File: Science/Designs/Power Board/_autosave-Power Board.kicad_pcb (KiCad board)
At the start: 2 copper layers, 114.3 x 90.2 mm, 27 parts, among them P1 PWR_IN, P2 MOTOR_PWR_OUT, P3 MAIN_PWR_OUT, P4 I2C, P5 MOTOR_SW, P6 REG_12V, P7 REG_5V, U1 INA219, U2 INA219, U3 INA219

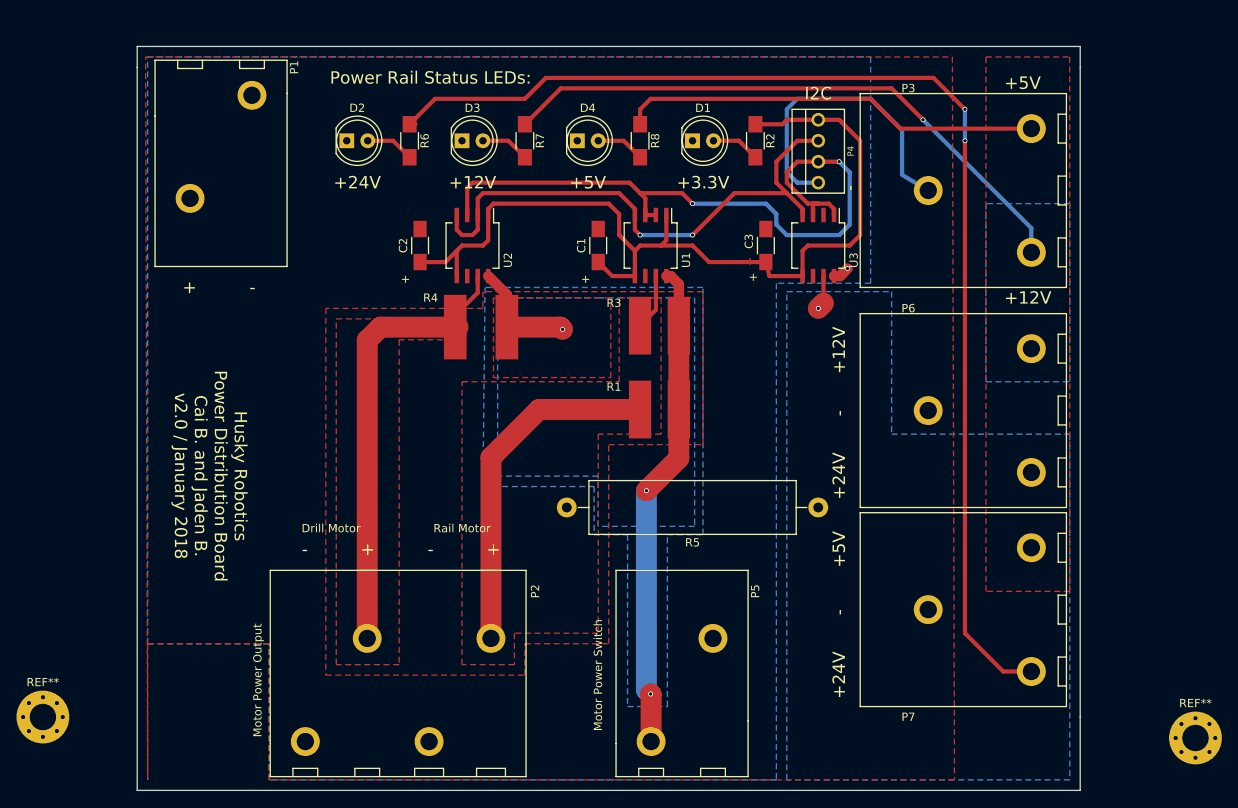
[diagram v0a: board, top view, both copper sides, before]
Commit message: Added mounting holes
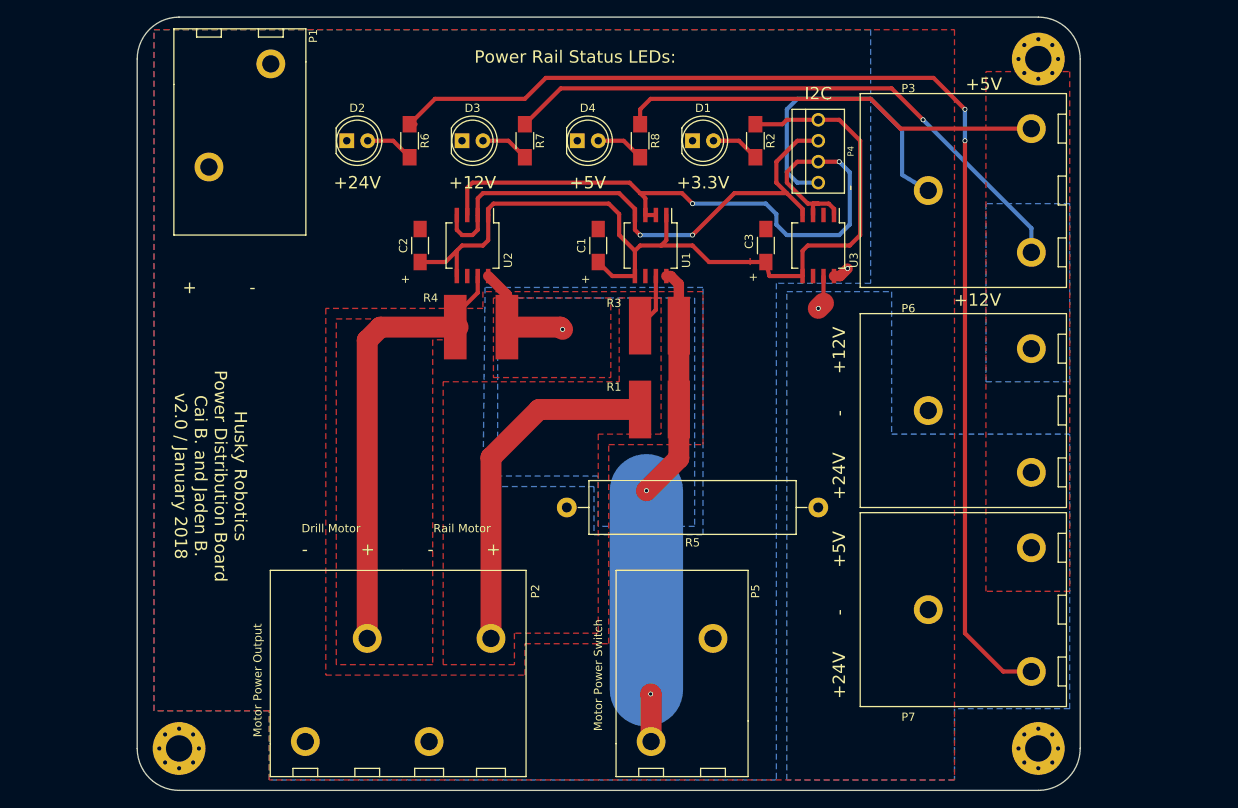
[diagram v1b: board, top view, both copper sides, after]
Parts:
- added REF**: MountingHole_3.2mm_M3_Pad_Via, Mounting_Holes:MountingHole_3.2mm_M3_Pad_Via, F.Cu at (182.9, 29.5)
- moved REF** 19.1 mm to (182.9, 113.0)
- moved REF** 16.9 mm to (78.7, 113.0)
- moved P1 4.44 mm to (86.1, 50.8)
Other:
- board size 114.3 x 90.2 mm -> 114.3 x 93.7 mm
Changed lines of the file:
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@@
     (links 60)
     (no_connects 0)
-    (area 73.584999 27.864999 188.035001 118.185001)
+    (area 73.584999 24.308999 188.035001 118.185001)
     (thickness 1.6)
-    (drawings 41)
+    (drawings 38)
     (tracks 172)
     (zones 0)
-    (modules 27)
+    (modules 28)
     (nets 16)
   )
@@
   (layers
     (0 F.Cu signal)
-    (31 B.Cu signal hide)
+    (31 B.Cu signal)
     (32 B.Adhes user hide)
     (33 F.Adhes user hide)
@@
   )
   (setup
-    (last_trace_width 2.54)
+    (last_trace_width 8.89)
     (user_trace_width 1.27)
     (user_trace_width 2.54)
@@
   )
   (module ScienceFootprints:PHOENIX_1792229 (layer F.Cu)
-    (at 83.82 54.61 180)
+    (at 86.106 50.8 180)
     (fp_text reference P1 (at -8.89 24.13 270) (layer F.SilkS)
       (effects (font (size 1 1) (thickness 0.15)))
@@
   )
   (module Mounting_Holes:MountingHole_3.2mm_M3_Pad_Via (layer F.Cu)
-    (at 62.23 109.22)
+    (at 78.74 113.03)
     (descr "Mounting Hole 3.2mm, M3")
     (tags "mounting hole 3.2mm m3")
     (attr virtual)
-    (fp_text reference REF** (at 0 -4.2) (layer F.SilkS)
+    (fp_text reference REF** (at 0 -4.2) (layer F.SilkS) hide
       (effects (font (size 1 1) (thickness 0.15)))
     )
@@
   )
   (module Mounting_Holes:MountingHole_3.2mm_M3_Pad_Via (layer F.Cu)
-    (at 201.93 111.76)
+    (at 182.88 113.03)
     (descr "Mounting Hole 3.2mm, M3")
     (tags "mounting hole 3.2mm m3")
     (attr virtual)
-    (fp_text reference REF** (at 0 -4.2) (layer F.SilkS)
+    (fp_text reference REF** (at 5.08 -2.794) (layer F.SilkS) hide
       (effects (font (size 1 1) (thickness 0.15)))
     )
@@
     (pad "" thru_hole circle (at 1.697056 -1.697056) (size 0.8 0.8) (drill 0.5) (layers *.Cu *.Mask))
   )
+  (module Mounting_Holes:MountingHole_3.2mm_M3_Pad_Via (layer F.Cu)
+    (at 182.88 29.464)
+    (descr "Mounting Hole 3.2mm, M3")
+    (tags "mounting hole 3.2mm m3")
+    (attr virtual)
+    (fp_text reference REF** (at 0 -4.2) (layer F.SilkS) hide
+      (effects (font (size 1 1) (thickness 0.15)))
+    )
+    (fp_text value MountingHole_3.2mm_M3_Pad_Via (at 0 4.2) (layer F.Fab)
+      (effects (font (size 1 1) (thickness 0.15)))
+    )
+    (fp_text user %R (at 0.3 0) (layer F.Fab)
+      (effects (font (size 1 1) (thickness 0.15)))
+    )
+    (fp_circle (center 0 0) (end 3.2 0) (layer Cmts.User) (width 0.15))
+    (fp_circle (center 0 0) (end 3.45 0) (layer F.CrtYd) (width 0.05))
+    (pad 1 thru_hole circle (at 0 0) (size 6.4 6.4) (drill 3.2) (layers *.Cu *.Mask))
+    (pad "" thru_hole circle (at 2.4 0) (size 0.8 0.8) (drill 0.5) (layers *.Cu *.Mask))
+    (pad "" thru_hole circle (at 1.697056 1.697056) (size 0.8 0.8) (drill 0.5) (layers *.Cu *.Mask))
+    (pad "" thru_hole circle (at 0 2.4) (size 0.8 0.8) (drill 0.5) (layers *.Cu *.Mask))
+    (pad "" thru_hole circle (at -1.697056 1.697056) (size 0.8 0.8) (drill 0.5) (layers *.Cu *.Mask))
+    (pad "" thru_hole circle (at -2.4 0) (size 0.8 0.8) (drill 0.5) (layers *.Cu *.Mask))
+    (pad "" thru_hole circle (at -1.697056 -1.697056) (size 0.8 0.8) (drill 0.5) (layers *.Cu *.Mask))
+    (pad "" thru_hole circle (at 0 -2.4) (size 0.8 0.8) (drill 0.5) (layers *.Cu *.Mask))
+    (pad "" thru_hole circle (at 1.697056 -1.697056) (size 0.8 0.8) (drill 0.5) (layers *.Cu *.Mask))
+  )
+  (gr_line (start 182.88 118.11) (end 78.74 118.11) (angle 90) (layer Edge.Cuts) (width 0.15))
+  (gr_line (start 187.96 29.464) (end 187.96 113.03) (angle 90) (layer Edge.Cuts) (width 0.15))
+  (gr_line (start 78.74 24.384) (end 182.88 24.384) (angle 90) (layer Edge.Cuts) (width 0.15))
+  (gr_line (start 73.66 113.03) (end 73.66 29.464) (angle 90) (layer Edge.Cuts) (width 0.15))
+  (gr_arc (start 78.74 29.464) (end 73.66 29.464) (angle 90) (layer Edge.Cuts) (width 0.15))
+  (gr_arc (start 182.88 29.464) (end 182.88 24.384) (angle 90) (layer Edge.Cuts) (width 0.15))
+  (gr_arc (start 182.88 113.03) (end 187.96 113.03) (angle 90) (layer Edge.Cuts) (width 0.15))
+  (gr_arc (start 78.74 113.03) (end 78.74 118.11) (angle 90) (layer Edge.Cuts) (width 0.15))
   (gr_text "Rail Motor" (at 113.03 86.36) (layer F.SilkS)
     (effects (font (size 1 1) (thickness 0.2)))
@@
     (effects (font (size 1.5 1.5) (thickness 0.3)))
   )
-  (gr_text "Power Rail Status LEDs:" (at 109.22 31.75) (layer F.SilkS)
+  (gr_text "Power Rail Status LEDs:" (at 126.746 29.21) (layer F.SilkS)
     (effects (font (size 1.5 1.5) (thickness 0.3)))
   )
@@
     (effects (font (size 1.5 1.5) (thickness 0.3)))
   )
-  (gr_text +12V (at 181.61 58.42) (layer F.SilkS)
-    (effects (font (size 1.5 1.5) (thickness 0.3)))
-  )
-  (gr_text +5V (at 180.975 32.385) (layer F.SilkS)
+  (gr_text +12V (at 175.514 58.674) (layer F.SilkS)
+    (effects (font (size 1.5 1.5) (thickness 0.3)))
+  )
+  (gr_text +5V (at 176.276 32.512) (layer F.SilkS)
     (effects (font (size 1.5 1.5) (thickness 0.3)))
   )
@@
     (effects (font (size 1.5 1.5) (thickness 0.3)))
   )
-  (gr_line (start 187.96 30.48) (end 187.96 27.94) (angle 90) (layer Edge.Cuts) (width 0.15))
-  (gr_line (start 74.93 118.11) (end 76.2 118.11) (angle 90) (layer Edge.Cuts) (width 0.15))
-  (gr_line (start 74.93 118.11) (end 73.66 118.11) (angle 90) (layer Edge.Cuts) (width 0.15))
-  (gr_line (start 73.66 27.94) (end 76.2 27.94) (angle 90) (layer Edge.Cuts) (width 0.15))
-  (gr_line (start 73.66 30.48) (end 73.66 27.94) (angle 90) (layer Edge.Cuts) (width 0.15))
-  (gr_line (start 73.66 118.11) (end 73.66 30.48) (angle 90) (layer Edge.Cuts) (width 0.15))
-  (gr_line (start 87.63 118.11) (end 76.2 118.11) (angle 90) (layer Edge.Cuts) (width 0.15))
-  (gr_line (start 187.96 118.11) (end 87.63 118.11) (angle 90) (layer Edge.Cuts) (width 0.15))
-  (gr_line (start 187.96 109.22) (end 187.96 118.11) (angle 90) (layer Edge.Cuts) (width 0.15))
-  (gr_line (start 187.96 30.48) (end 187.96 109.22) (angle 90) (layer Edge.Cuts) (width 0.15))
-  (gr_line (start 76.2 27.94) (end 187.96 27.94) (angle 90) (layer Edge.Cuts) (width 0.15))
   (segment (start 107.95 54.07) (end 111.03 54.07) (width 0.508) (layer F.Cu) (net 1))
   (segment (start 111.03 54.07) (end 112.395 52.705) (width 0.508) (layer F.Cu) (net 1))
@@
   (segment (start 139.31 77.86) (end 135.382 81.788) (width 2.54) (layer F.Cu) (net 14))
   (segment (start 139.31 77.86) (end 139.31 71.94) (width 2.54) (layer F.Cu) (net 14))
-  (segment (start 135.382 105.918) (end 135.382 81.788) (width 2.54) (layer B.Cu) (net 14))
+  (segment (start 135.382 105.918) (end 135.382 81.788) (width 8.89) (layer B.Cu) (net 14))
   (segment (start 135.89 106.426) (end 135.382 105.918) (width 2.54) (layer B.Cu) (net 14))
   (via (at 135.89 106.426) (size 0.6) (drill 0.4) (layers F.Cu B.Cu) (net 14))
@@
     (polygon
       (pts
-        (xy 172.72 116.84) (xy 89.662 116.84) (xy 89.662 100.33) (xy 74.93 100.33) (xy 74.93 116.84)
-        (xy 74.676 29.21) (xy 172.466 29.21)
+        (xy 172.72 116.84) (xy 89.662 116.84) (xy 89.662 108.458) (xy 75.692 108.458) (xy 75.692 25.908)
+        (xy 172.72 25.908)
       )
     )
@@
     (polygon
       (pts
-        (xy 162.56 29.21) (xy 162.56 56.642) (xy 151.13 56.642) (xy 151.13 116.84) (xy 89.662 116.84)
-        (xy 89.662 100.33) (xy 74.93 100.33) (xy 74.93 29.21)
+        (xy 162.56 25.908) (xy 162.56 56.642) (xy 151.13 56.642) (xy 151.13 116.84) (xy 89.662 116.84)
+        (xy 89.662 108.458) (xy 75.692 108.458) (xy 75.692 25.908)
       )
     )
@@
     (polygon
       (pts
-        (xy 165.1 74.93) (xy 186.69 74.93) (xy 186.69 116.84) (xy 152.4 116.84) (xy 152.4 76.2)
-        (xy 152.4 57.658) (xy 165.1 57.658)
+        (xy 172.72 116.84) (xy 152.4 116.84) (xy 152.4 57.658) (xy 165.1 57.658) (xy 165.1 74.93)
+        (xy 186.69 74.93) (xy 186.69 108.204) (xy 172.72 108.204)
       )
     )
@@
     (polygon
       (pts
-        (xy 176.53 29.21) (xy 186.69 29.21) (xy 186.69 93.98) (xy 176.53 93.98)
+        (xy 176.53 30.988) (xy 186.69 30.988) (xy 186.69 93.98) (xy 176.53 93.98)
       )
     )
@@
     (polygon
       (pts
-        (xy 113.03 60.96) (xy 113.03 63.5) (xy 105.41 63.5) (xy 105.41 102.87) (xy 97.79 102.87)
+        (xy 113.03 60.96) (xy 113.03 63.5) (xy 109.474 63.5) (xy 109.474 102.87) (xy 97.79 102.87)
         (xy 97.79 60.96)
       )
@@
       (pts
         (xy 137.16 74.93) (xy 129.54 74.93) (xy 129.54 99.06) (xy 119.38 99.06) (xy 119.38 102.87)
-        (xy 113.03 102.87) (xy 113.03 68.58) (xy 132.08 68.58) (xy 132.08 58.42) (xy 137.16 58.42)
+        (xy 110.744 102.87) (xy 110.744 68.58) (xy 132.08 68.58) (xy 132.08 58.42) (xy 137.16 58.42)
       )
     )
